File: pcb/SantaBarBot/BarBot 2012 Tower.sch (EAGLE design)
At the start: 8 parts, among them J1 AVR_SPI_PRG_62X3_LOCK, U1 ATMEGA328P, U2 L298_BRIDGE_DRIVER

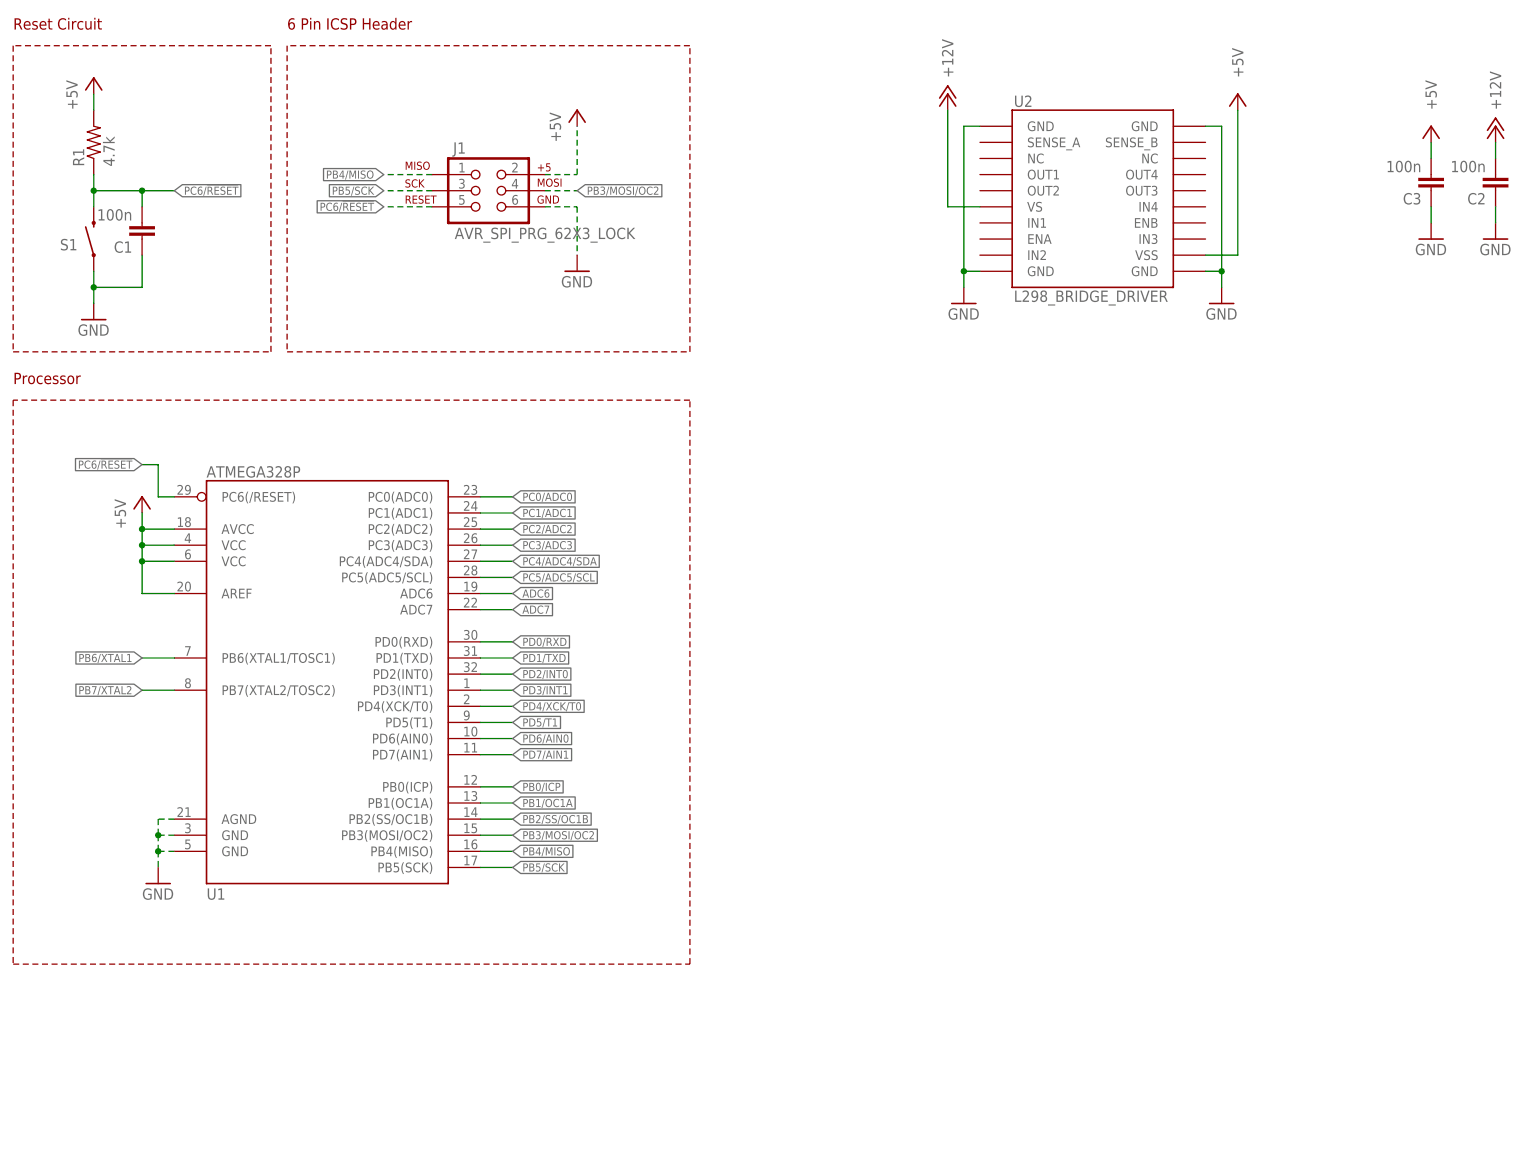
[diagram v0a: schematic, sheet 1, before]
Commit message: Created new component for dual invert chip.  Mostly done with motor driver, need to add sense resistors.  Added SPI buffer resistors
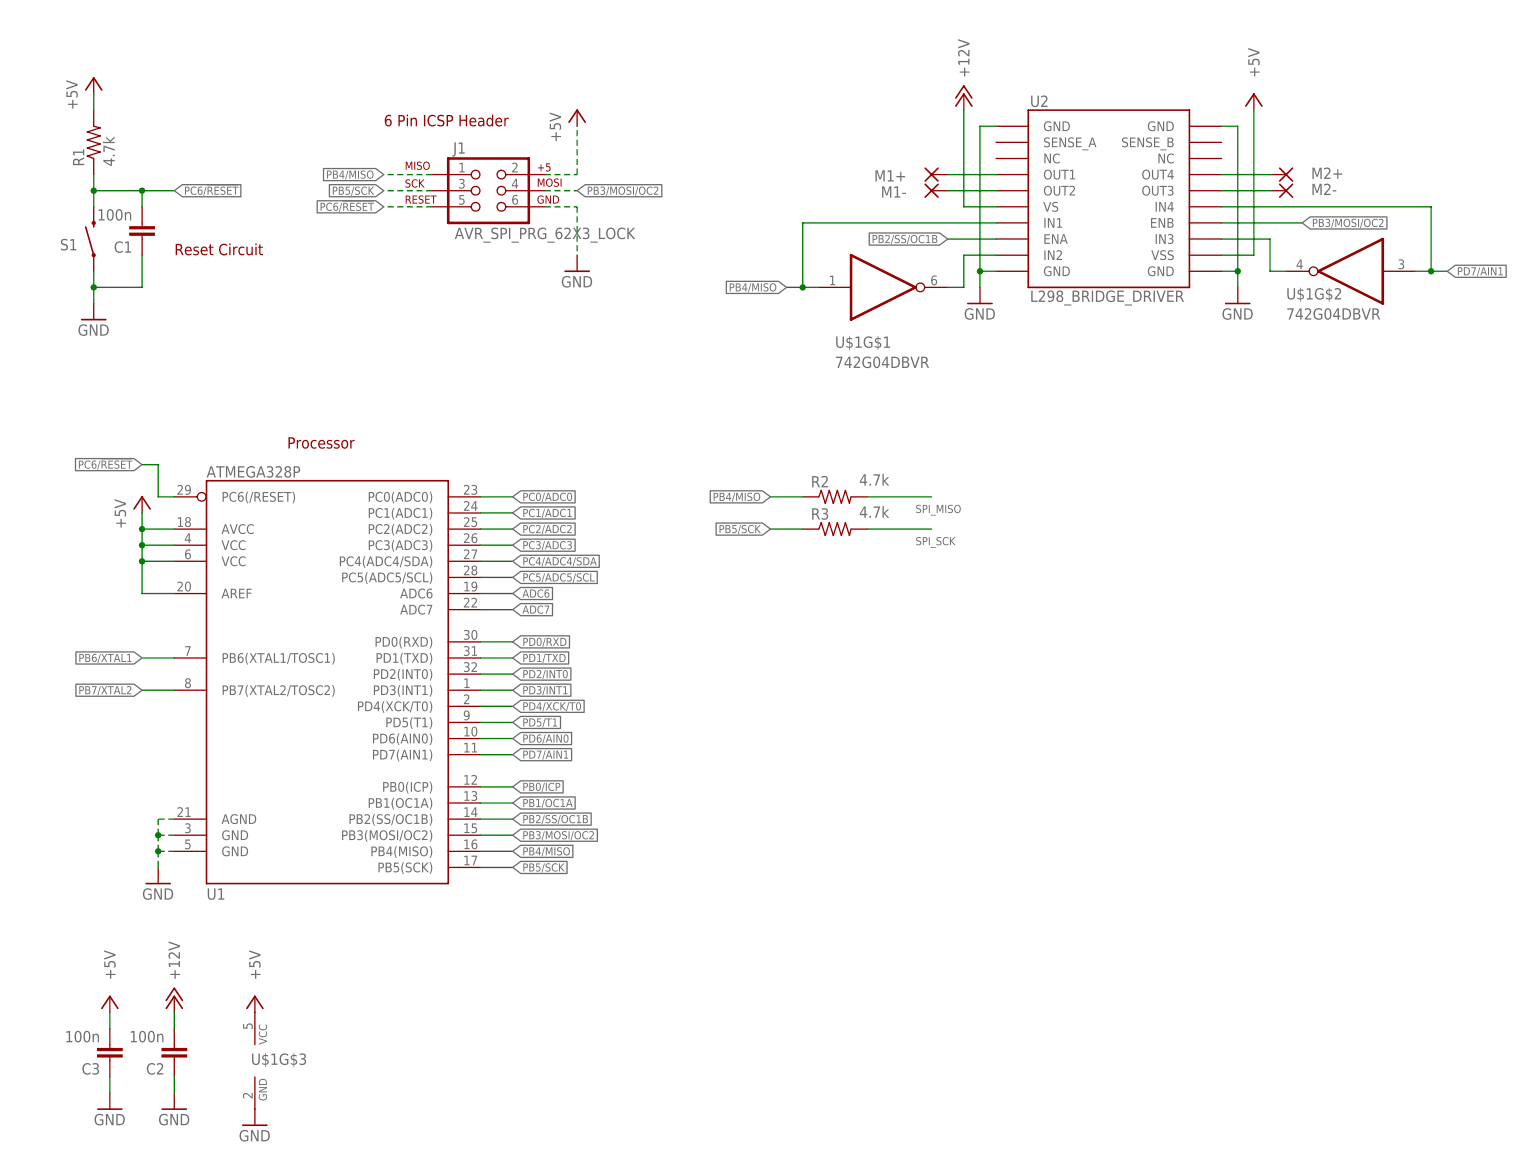
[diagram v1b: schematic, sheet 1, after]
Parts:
- added M1+, M1-, M2+, M2-: (no value), wirepad:3,81/1,4
- added R2, R3: 4.7k, rcl:R-US_R2012
- added U$1: 742G04DBVR, 74xx-little-us:742G04DBVR
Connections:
- new net N$1: U$1G$1.O, U2.IN2
- new net N$2: M1+.P, U2.OUT1
- new net N$3: U$1G$2.O, U2.IN3
- new net N$4: M1-.P, U2.OUT2
- new net N$5: M2+.P, U2.OUT4
- new net N$6: M2-.P, U2.OUT3
- new net SPI_MISO: R2.2
- new net SPI_SCK: R3.2
- net +5V: now also U$1G$3.VCC
- net GND: now also U$1G$3.GND
- net PB2/SS/OC1B: now also U2.ENA
- net PB3/MOSI/OC2: now also U2.ENB
- net PB4/MISO: now also R2.1, U$1G$1.I, U2.IN1
- net PB5/SCK: now also R3.1
- net PD7/AIN1: now also U$1G$2.I, U2.IN4
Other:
- moved on the sheet: C2, C3, U2
